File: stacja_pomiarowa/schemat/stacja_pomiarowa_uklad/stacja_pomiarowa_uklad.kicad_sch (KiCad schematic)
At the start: 40 parts, among them J1 Conn_02x17_Counter_Clockwise, J2 Conn_02x08_Counter_Clockwise, J3 Conn_01x01, J4 Conn_02x04_Counter_Clockwise, J5 Conn_01x02, J6 Conn_01x02, Q1 NPN, U1 CD4051B, U2 CD4051B, U3 ESP DevKitV1, U4 ADS1115, U5 CD4051B, U6 CD4051B, U7 MCP23017_SP, U8 CD4051B

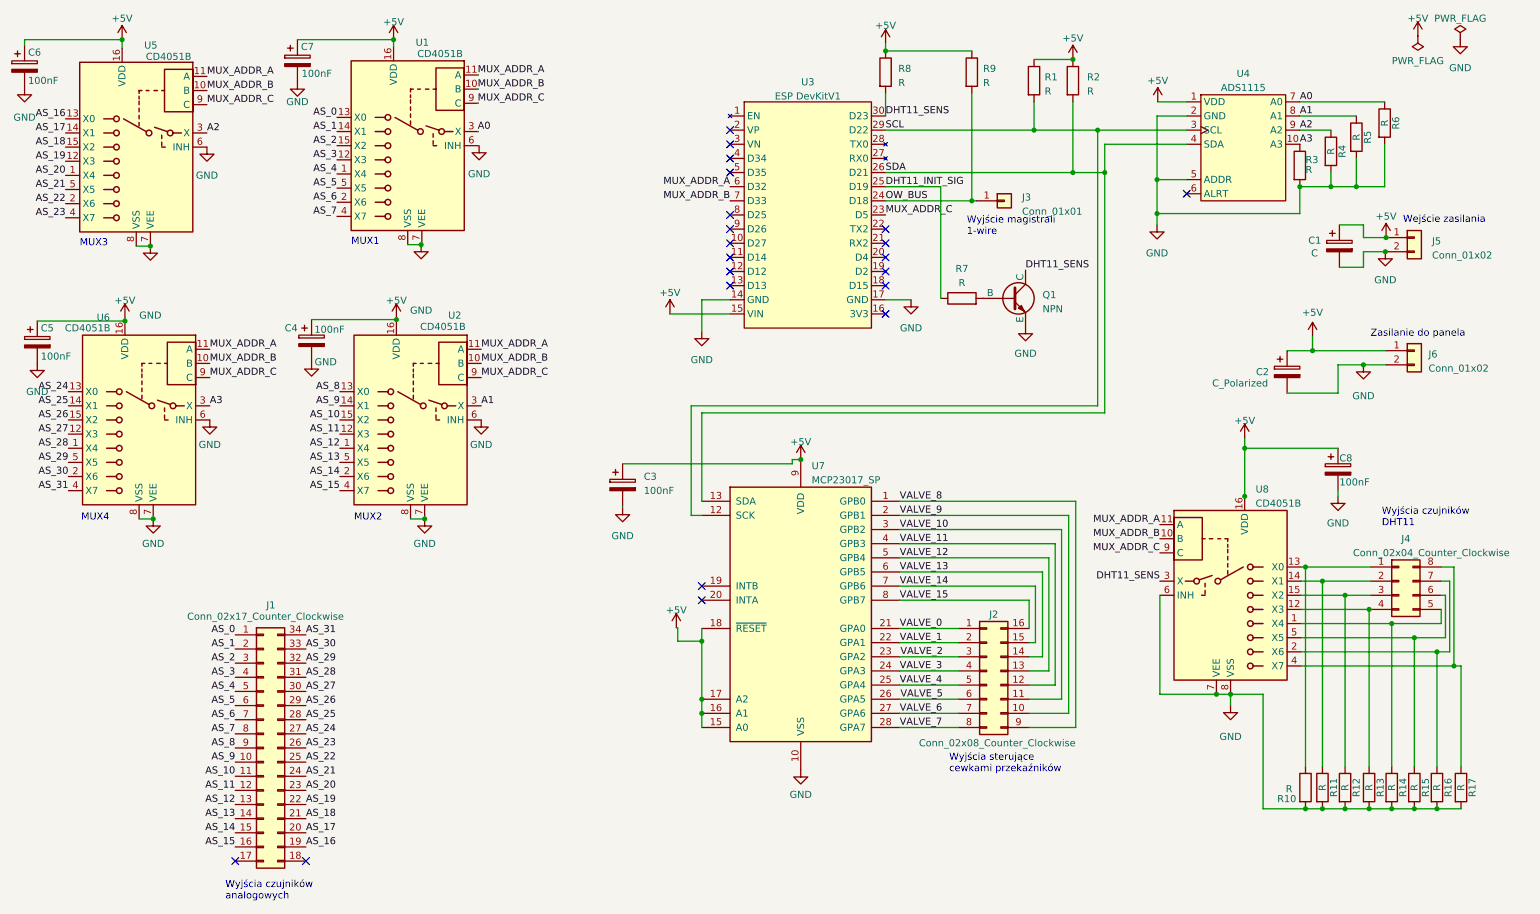
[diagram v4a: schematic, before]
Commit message: Dodano ledy informujące czy urządzenie połączyło się z systemem, dodane tytuły podschematów ze złączami
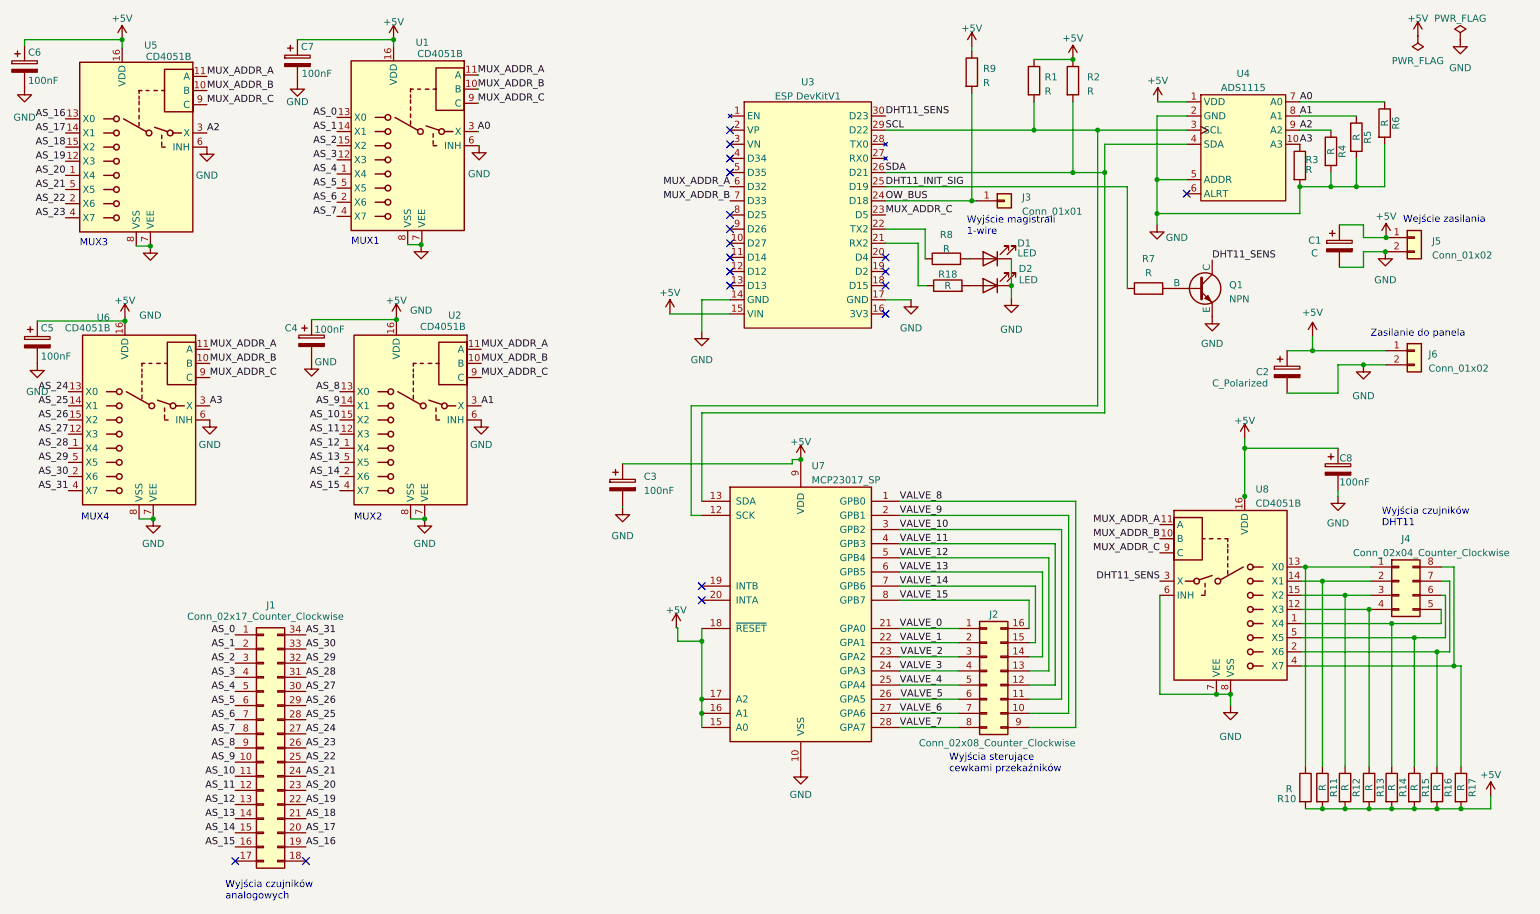
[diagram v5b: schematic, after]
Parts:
- added D1, D2: LED, symbol Device:LED
- added R18: R, symbol Device:R
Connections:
- net +5V: now also R10.2, R11.2, R12.2, R13.2, R14.2, R15.2, R16.2, R17.2; no longer R8.1
- net DHT11_SENS: no longer R8.2
- net GND: now also D1.1 (K), D2.1 (K); no longer R10.2, R11.2, R12.2, R13.2, R14.2, R15.2, R16.2, R17.2
- net at U3.21 (RX2): now also R18.1
- net at U3.22 (TX2): now also R8.1
- new net: D2.2 (A), R18.2
- new net: D1.2 (A), R8.2
- no-connect marks 21 -> 19
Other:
- moved on the sheet: Q1, R7
